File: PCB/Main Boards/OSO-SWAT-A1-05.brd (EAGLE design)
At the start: 24.4 x 24.4 mm, 36 parts, among them J1 FH19C-9S-0.5SH_10_, U1 ATSAML22J18A-MUT, U2 MIC5365-3.3YC5-TR, X1 32.768

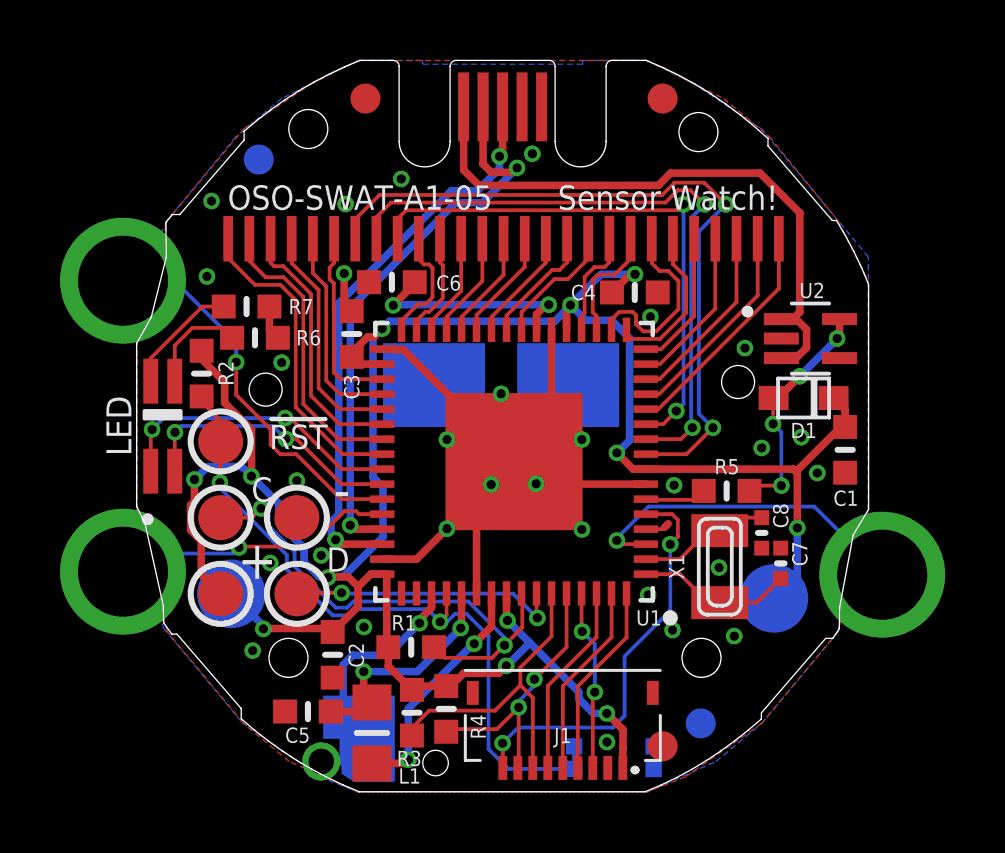
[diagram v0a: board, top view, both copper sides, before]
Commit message: fatten GND wire to USB port
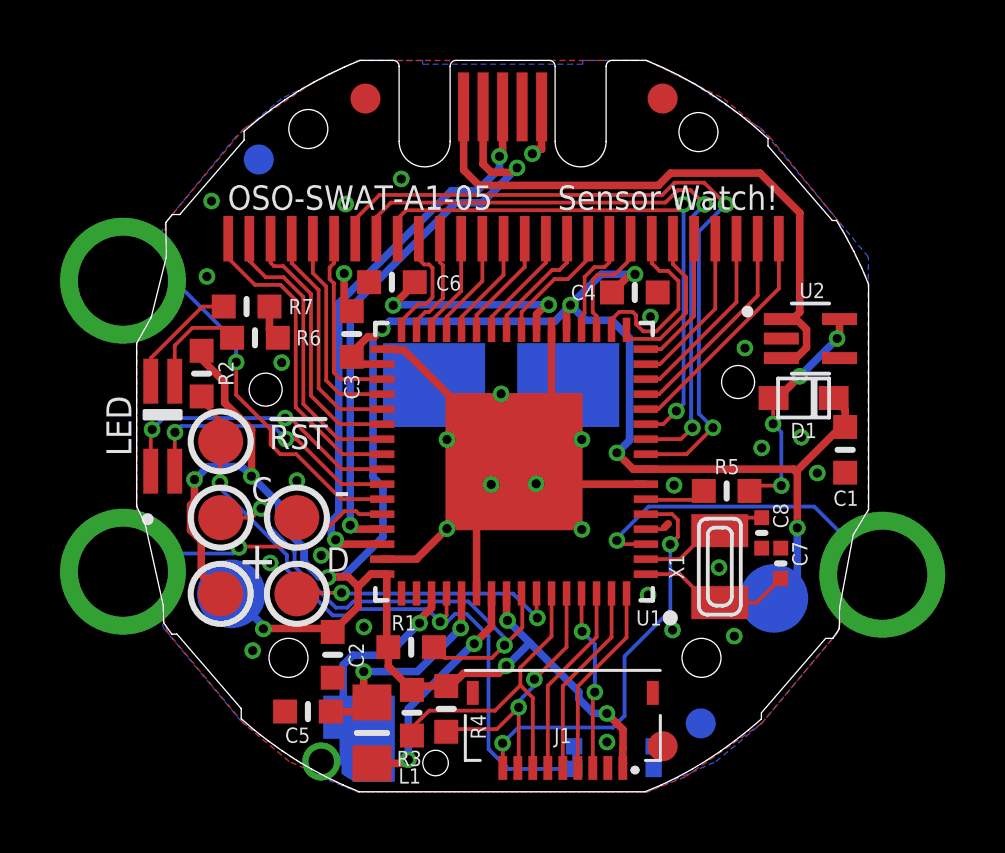
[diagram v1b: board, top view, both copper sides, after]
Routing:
- net GND: track 23.1 -> 25.0 mm
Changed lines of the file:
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@@
 <via x="19.9136" y="5.1943" extent="1-16" drill="0.3048"/>
 <via x="17.907" y="10.2235" extent="1-16" drill="0.3048"/>
+<wire x1="13.492" y1="22.836440625" x2="13.492" y2="21.4249" width="0.254" layer="1"/>
+<wire x1="13.492" y1="21.4249" x2="13.2334" y2="21.4249" width="0.254" layer="1"/>
+<wire x1="13.2334" y1="21.4249" x2="13.1826" y2="21.3741" width="0.254" layer="1"/>
+<wire x1="13.1826" y1="21.3741" x2="13.1826" y2="21.2725" width="0.254" layer="1"/>
 </signal>
 <signal name="!RESET">
